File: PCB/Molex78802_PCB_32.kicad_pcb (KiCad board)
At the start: 2 copper layers, 16.5 x 43.1 mm, 1 part

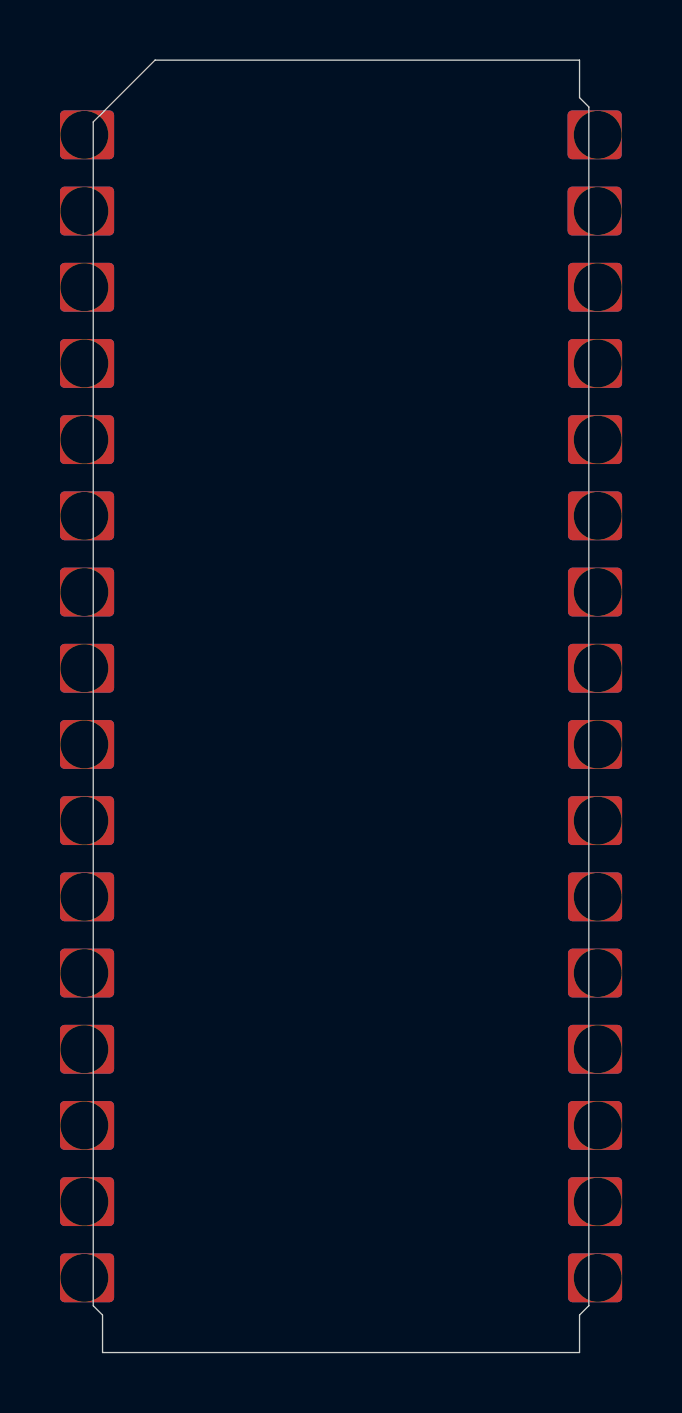
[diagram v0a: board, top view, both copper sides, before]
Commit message: improved fitment all around, simplified the pcb corners, removed junk from the scad model
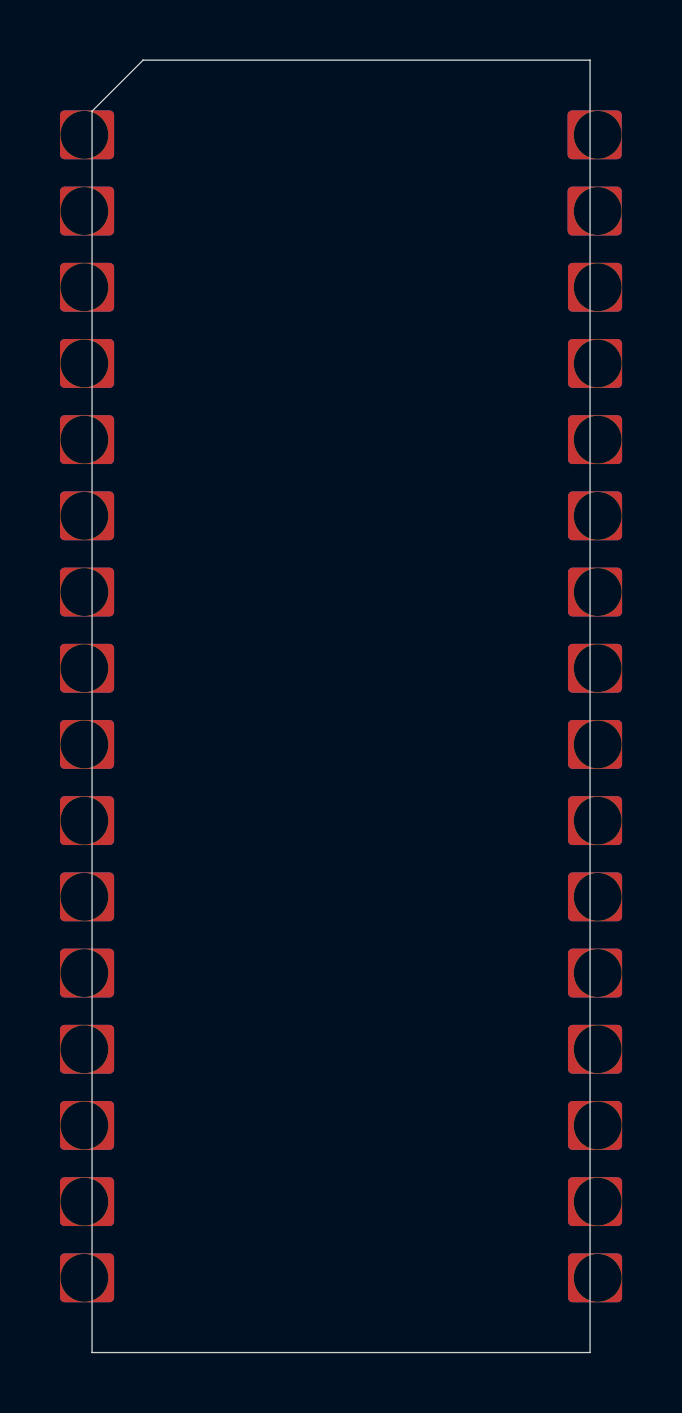
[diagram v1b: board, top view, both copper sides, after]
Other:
- board size 16.5 x 43.1 mm -> 16.6 x 43.1 mm
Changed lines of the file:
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@@
   (general
     (thickness 1.6)
-    (drawings 11)
+    (drawings 5)
     (tracks 0)
     (zones 0)
@@
     (title "Molex78802 PCB 28")
     (date 2021-05-20)
-    (rev 004)
+    (rev 005)
     (company b.kenyon.w@gmail.com)
   )
@@
       (effects (font (size 1.2065 1.2065) (thickness 0.1016)) (justify bottom))
     )
-    (fp_text user "0.7 border on bottom - 41.68 x 14.4 x 1.4 usable bottom" (at -5.5 -19.54) (layer Dwgs.User)
-      (effects (font (size 0.25 0.25) (thickness 0.02)) (justify left))
-    )
-    (fp_text user "10.0 x 1.0 retainer wedges on top" (at -3.5 -20.04) (layer Dwgs.User)
-      (effects (font (size 0.25 0.25) (thickness 0.02)) (justify left))
-    )
-    (fp_text user "Castellation depth 0.5mm min" (at 6.35 0 -90) (layer Dwgs.User)
-      (effects (font (size 1 1) (thickness 0.1)))
-    )
-    (fp_text user "Board outline: 0.01mm grid, copy Eco2.User" (at -6 0 -90) (layer Eco2.User)
-      (effects (font (size 1 1) (thickness 0.1)))
-    )
-    (fp_text user "Eco1.User is Edge.Cuts for use without carrier." (at -4.445 0 -90) (layer Eco1.User)
-      (effects (font (size 0.8 0.8) (thickness 0.05)))
-    )
     (fp_poly (pts (xy 9.2156 18.3896) (xy 7.717 18.3896) (xy 7.717 19.7104) (xy 9.2156 19.7104)) (layer Bottom) (width 0.3048))
     (fp_poly (pts (xy 9.2156 19.7104) (xy 7.717 19.7104) (xy 7.717 18.3896) (xy 9.2156 18.3896)) (layer Top) (width 0.3048))
@@
     (fp_line (start -6 -19.54) (end -5.5 -19.54) (layer Dwgs.User) (width 0.01))
     (fp_line (start -6 -20.84) (end -6 -19.54) (layer Dwgs.User) (width 0.01))
-    (fp_line (start 7.2 -20.84) (end 7.2 20.84) (layer Dwgs.User) (width 0.01))
-    (fp_line (start -7.2 -20.84) (end -7.2 20.84) (layer Dwgs.User) (width 0.01))
-    (fp_line (start -7.2 -20.84) (end 7.2 -20.84) (layer Dwgs.User) (width 0.01))
-    (fp_line (start -7.2 20.84) (end 7.2 20.84) (layer Dwgs.User) (width 0.01))
-    (fp_line (start -8.255 0.0508) (end -8.255 -0.0508) (layer Dwgs.User) (width 0.002))
+    (fp_line (start 7.6 -20.84) (end 7.6 20.84) (layer Dwgs.User) (width 0.01))
+    (fp_line (start -7.6 -20.84) (end -7.6 20.84) (layer Dwgs.User) (width 0.01))
+    (fp_line (start -7.6 -20.84) (end 7.6 -20.84) (layer Dwgs.User) (width 0.01))
+    (fp_line (start -7.6 20.84) (end 7.6 20.84) (layer Dwgs.User) (width 0.01))
     (fp_poly (pts (xy 9.2156 1.9304) (xy 7.717 1.9304) (xy 7.717 0.6096) (xy 9.2156 0.6096)) (layer Top) (width 0.3048))
     (fp_poly (pts (xy 9.2156 -0.6096) (xy 7.717 -0.6096) (xy 7.717 -1.9304) (xy 9.2156 -1.9304)) (layer Top) (width 0.3048))
@@
     (fp_line (start -0.762 -24.13) (end 0.762 -24.13) (layer Eco1.User) (width 0.01))
     (fp_line (start -0.762 -21.59) (end -0.762 -24.13) (layer Eco1.User) (width 0.01))
-    (fp_line (start -7.95 21.54) (end 7.95 21.54) (layer Eco2.User) (width 0.01))
-    (fp_line (start 7.95 21.54) (end 7.95 20.29) (layer Eco2.User) (width 0.01))
-    (fp_line (start -7.95 21.54) (end -7.95 20.29) (layer Eco2.User) (width 0.01))
-    (fp_line (start 7.95 -20.29) (end 7.95 -21.54) (layer Eco2.User) (width 0.01))
-    (fp_line (start 8.26 19.98) (end 8.26 -19.98) (layer Eco2.User) (width 0.01))
-    (fp_line (start -8.26 19.98) (end -8.26 -19.48) (layer Eco2.User) (width 0.01))
-    (fp_line (start 7.95 -21.54) (end -6.2 -21.54) (layer Eco2.User) (width 0.01))
-    (fp_line (start -6.2 -21.54) (end -8.26 -19.48) (layer Eco2.User) (width 0.01))
+    (fp_line (start -8.3 21.54) (end 8.3 21.54) (layer Eco2.User) (width 0.01))
+    (fp_line (start 8.3 21.54) (end 8.3 -21.54) (layer Eco2.User) (width 0.01))
+    (fp_line (start -8.3 21.54) (end -8.3 -19.84) (layer Eco2.User) (width 0.01))
     (fp_line (start 7.75716 17.78) (end 7.75716 12.7) (layer Dwgs.User) (width 0.01))
-    (fp_line (start 6.35 12.065) (end 6.35 15.24) (layer Dwgs.User) (width 0.05))
-    (fp_line (start 6.35 15.24) (end 7.747 15.24) (layer Dwgs.User) (width 0.05))
-    (fp_line (start 7.747 15.24) (end 7.467 15.52) (layer Dwgs.User) (width 0.05))
-    (fp_line (start 7.467 14.96) (end 7.747 15.24) (layer Dwgs.User) (width 0.05))
-    (fp_line (start 8.27 15.24) (end 8.55 15.52) (layer Dwgs.User) (width 0.05))
-    (fp_line (start 8.55 14.96) (end 8.27 15.24) (layer Dwgs.User) (width 0.05))
-    (fp_line (start 8.27 15.24) (end 9.667 15.24) (layer Dwgs.User) (width 0.05))
+    (fp_line (start 6.34 12.065) (end 6.34 15.24) (layer Dwgs.User) (width 0.05))
+    (fp_line (start 6.34 15.24) (end 7.737 15.24) (layer Dwgs.User) (width 0.05))
+    (fp_line (start 7.737 15.24) (end 7.457 15.52) (layer Dwgs.User) (width 0.05))
+    (fp_line (start 7.457 14.96) (end 7.737 15.24) (layer Dwgs.User) (width 0.05))
+    (fp_line (start 8.32 15.24) (end 8.6 15.52) (layer Dwgs.User) (width 0.05))
+    (fp_line (start 8.6 14.96) (end 8.32 15.24) (layer Dwgs.User) (width 0.05))
+    (fp_line (start 8.32 15.24) (end 9.717 15.24) (layer Dwgs.User) (width 0.05))
     (fp_line (start -5 -21.54) (end -5 -20.54) (layer Dwgs.User) (width 0.01))
     (fp_line (start -5 -20.54) (end 5 -20.54) (layer Dwgs.User) (width 0.01))
@@
     (fp_line (start -5 20.54) (end 5 20.54) (layer Dwgs.User) (width 0.01))
     (fp_line (start -5 21.54) (end 5 21.54) (layer Dwgs.User) (width 0.01))
-    (fp_line (start -7.95 20.29) (end -8.26 19.98) (layer Eco2.User) (width 0.01))
-    (fp_line (start 7.95 20.29) (end 8.26 19.98) (layer Eco2.User) (width 0.01))
-    (fp_line (start 7.95 -20.29) (end 8.26 -19.98) (layer Eco2.User) (width 0.01))
+    (fp_line (start -6.6 -21.54) (end 8.3 -21.54) (layer Eco2.User) (width 0.01))
+    (fp_line (start -6.6 -21.54) (end -8.3 -19.84) (layer Eco2.User) (width 0.01))
+    (fp_text user "0.7 border on bottom - 41.48 x 15 x 1.4 usable bottom" (at -5.5 -19.54) (layer Dwgs.User)
+      (effects (font (size 0.25 0.25) (thickness 0.02)) (justify left))
+    )
+    (fp_text user "10.0 x 1.0 retainer wedges on top" (at -3.5 -20.04) (layer Dwgs.User)
+      (effects (font (size 0.25 0.25) (thickness 0.02)) (justify left))
+    )
+    (fp_text user "Castellation depth 0.5mm min" (at 6.35 0 -90) (layer Dwgs.User)
+      (effects (font (size 1 1) (thickness 0.1)))
+    )
+    (fp_text user "Board outline: 0.01mm grid, copy Eco2.User" (at -6 0 -90) (layer Eco2.User)
+      (effects (font (size 1 1) (thickness 0.1)))
+    )
+    (fp_text user "Eco1.User is Edge.Cuts for use without carrier." (at -4.445 0 -90) (layer Eco1.User)
+      (effects (font (size 0.8 0.8) (thickness 0.05)))
+    )
     (pad 17 thru_hole circle (at 8.5552 19.05 180) (size 1.6002 1.6002) (drill 1.59766) (layers *.Cu *.Mask))
     (pad 16 thru_hole circle (at -8.5552 19.05) (size 1.6002 1.6002) (drill 1.59766) (layers *.Cu *.Mask)
@@
     (pad 18 thru_hole circle (at 8.5552 16.51 180) (size 1.6002 1.6002) (drill 1.59766) (layers *.Cu *.Mask))
     (model ${KIPRJMOD}/000_LOCAL.pretty/3d/Molex78802_PCB_32.step
-      (offset (xyz 0 0 -0.18))
+      (offset (xyz 0 0 -0.16))
       (scale (xyz 1 1 1))
       (rotate (xyz 0 0 90))
     )
   )
-  (gr_line (start 139.2684 119.477) (end 138.9584 119.167) (layer Edge.Cuts) (width 0.01))
-  (gr_line (start 155.1684 119.477) (end 155.4784 119.167) (layer Edge.Cuts) (width 0.01))
-  (gr_line (start 155.1684 78.897) (end 155.4784 79.207) (layer Edge.Cuts) (width 0.01))
-  (gr_line (start 139.2684 119.477) (end 139.2684 120.727) (layer Edge.Cuts) (width 0.01))
-  (gr_line (start 138.9584 79.707) (end 138.9584 119.167) (layer Edge.Cuts) (width 0.01))
-  (gr_line (start 141.0184 77.647) (end 138.9584 79.707) (layer Edge.Cuts) (width 0.01))
-  (gr_line (start 155.1684 77.647) (end 141.0184 77.647) (layer Edge.Cuts) (width 0.01))
-  (gr_line (start 155.1684 78.897) (end 155.1684 77.647) (layer Edge.Cuts) (width 0.01))
-  (gr_line (start 155.4784 119.167) (end 155.4784 79.207) (layer Edge.Cuts) (width 0.01))
-  (gr_line (start 155.1684 120.727) (end 155.1684 119.477) (layer Edge.Cuts) (width 0.01))
-  (gr_line (start 139.2684 120.727) (end 155.1684 120.727) (layer Edge.Cuts) (width 0.01))
+  (gr_line (start 138.9184 79.347) (end 140.6184 77.647) (layer Edge.Cuts) (width 0.01))
+  (gr_line (start 138.9184 120.727) (end 138.9184 79.347) (layer Edge.Cuts) (width 0.01))
+  (gr_line (start 155.5184 77.647) (end 155.5184 120.727) (layer Edge.Cuts) (width 0.01))
+  (gr_line (start 155.5184 77.647) (end 140.6184 77.647) (layer Edge.Cuts) (width 0.01))
+  (gr_line (start 138.9184 120.727) (end 155.5184 120.727) (layer Edge.Cuts) (width 0.01))
 )
